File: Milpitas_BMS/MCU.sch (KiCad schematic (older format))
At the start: 74 parts, among them J100 JTAG, J101 DIAGS_UART, J102 CAN_CONN, SW100 SW_SPST, SW101 SW_SPST, U100 MIC5283-3.3ML-TR, U101 STM32F303RETx, U102 SN65HVD232

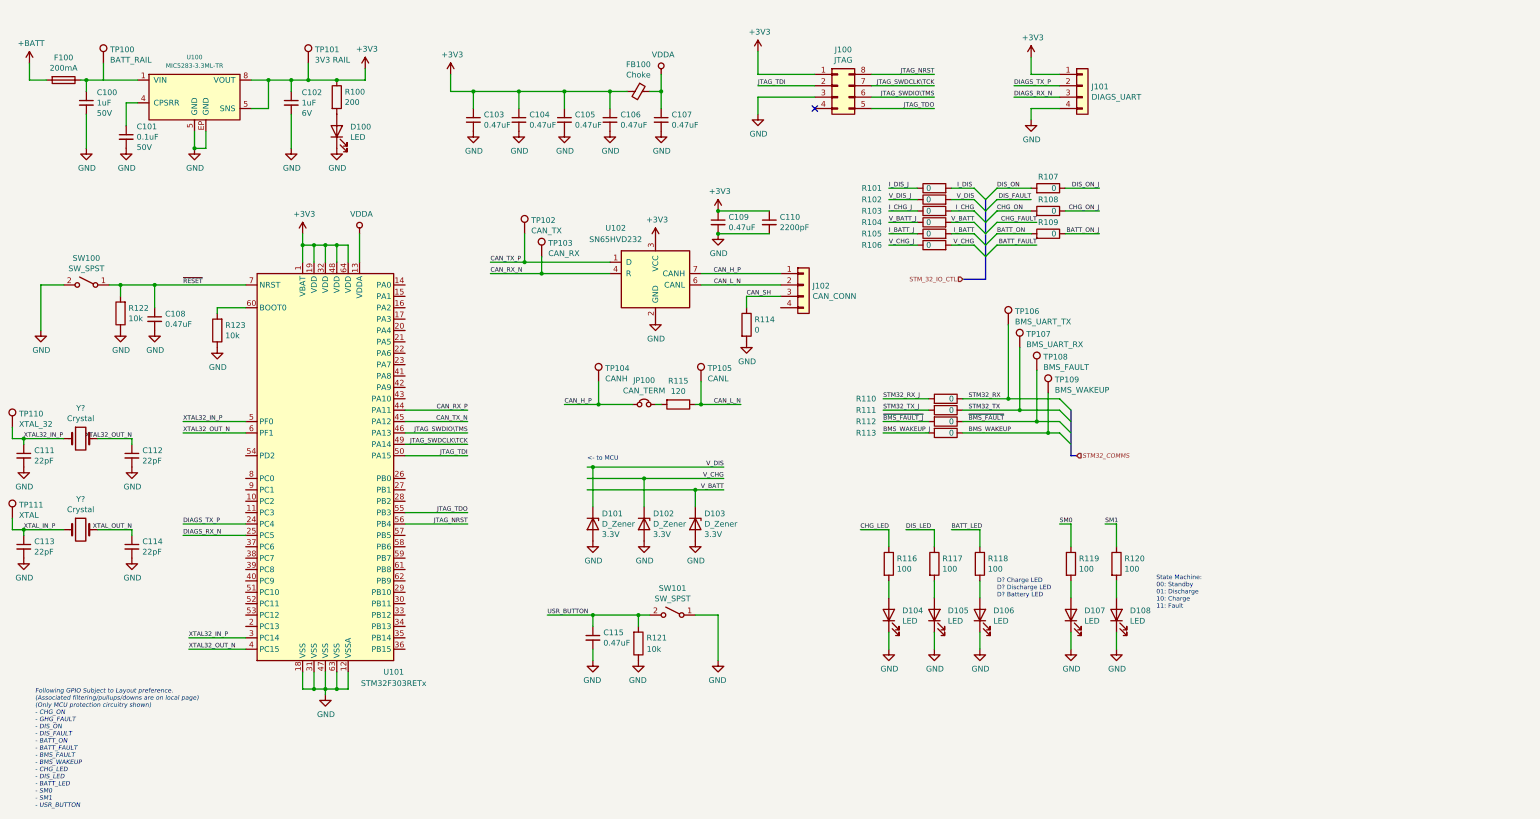
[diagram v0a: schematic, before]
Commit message: updated some parts to inclued footprints + digikey P/N
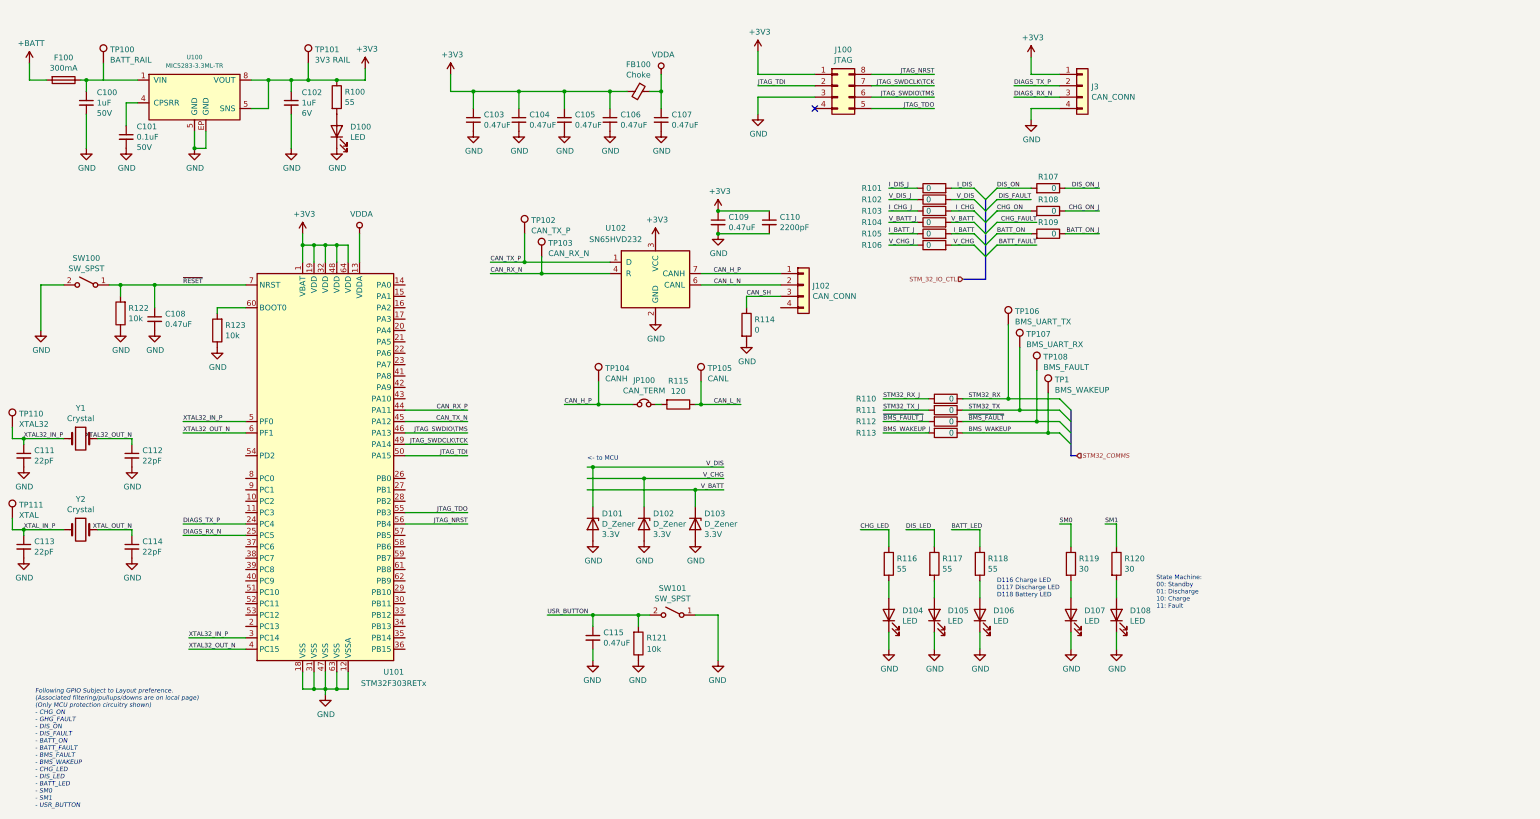
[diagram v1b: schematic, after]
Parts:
- removed J101: DIAGS_UART, symbol Connector_Generic:Conn_01x04
- removed TP109: BMS_WAKEUP, symbol Connector:TestPoint
- added J3: CAN_CONN, Connector_PinHeader_1.27mm:PinHeader_2x02_P1.27mm_Vertical, symbol Connector_Generic:Conn_01x04
- added TP1: BMS_WAKEUP, TestPoint:TestPoint_Bridge_Pitch2.54mm_Drill1.0mm, symbol Connector:TestPoint
- C100, C101, C102, C103, C104, C105, C106, C107, C108, C109, C110, C115: footprint (none) -> Capacitor_SMD:C_0603_1608Metric
- D100, D104, D105, D106: footprint (none) -> LED_SMD:LED_0603_1608Metric; Digikey (none) -> SML-D12D1WT86CT-ND
- D107, D108: footprint (none) -> LED_SMD:LED_0603_1608Metric; Digikey (none) -> 732-4978-1-ND
- F100: value 200mA -> 300mA; footprint (none) -> Fuse:Fuse_0603_1608Metric; Digikey (none) -> 507-1087-1-ND
- FB100: footprint (none) -> Inductor_SMD:L_0603_1608Metric; Digikey (none) -> 445-8672-1-ND
- J100: footprint (none) -> Connector_PinHeader_1.27mm:PinHeader_2x04_P1.27mm_Vertical; Digikey (none) -> 2057-HPH2-A-08-UA-ND
- J102: footprint (none) -> Connector_PinHeader_1.27mm:PinHeader_2x02_P1.27mm_Vertical; Digikey (none) -> 2057-HPH2-A-04-UA-ND
- JP100: footprint (none) -> Jumper:SolderJumper-2_P1.3mm_Open_TrianglePad1.0x1.5mm
- R100: value 200 -> 55; footprint (none) -> Resistor_SMD:R_0603_1608Metric
- R101, R102, R103, R104, R105, R106, R107, R108, R109, R110, R111, R112, R113, R114, R115, R121, R122, R123: footprint (none) -> Resistor_SMD:R_0603_1608Metric
- R116, R117, R118: value 100 -> 55; footprint (none) -> Resistor_SMD:R_0603_1608Metric
- R119, R120: value 100 -> 30; footprint (none) -> Resistor_SMD:R_0603_1608Metric
- TP100, TP101, TP104, TP105, TP106, TP107, TP108, TP111: footprint (none) -> TestPoint:TestPoint_Bridge_Pitch2.54mm_Drill1.0mm; Digikey (none) -> 36-5003-ND
- TP102: value CAN_TX -> CAN_TX_P; footprint (none) -> TestPoint:TestPoint_Bridge_Pitch2.54mm_Drill1.0mm; Digikey (none) -> 36-5003-ND
- TP103: value CAN_RX -> CAN_RX_N; footprint (none) -> TestPoint:TestPoint_Bridge_Pitch2.54mm_Drill1.0mm; Digikey (none) -> 36-5003-ND
- TP110: value XTAL_32 -> XTAL32; footprint (none) -> TestPoint:TestPoint_Bridge_Pitch2.54mm_Drill1.0mm; Digikey (none) -> 36-5003-ND
- U100: footprint (none) -> Package_DFN_QFN:MLF-8-1EP_3x3mm_P0.65mm_EP1.55x2.3mm_ThermalVias; Digikey (none) -> MIC5283-3.3YML-CT-ND
- gave numbers to parts that had none: 2
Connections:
- net +3V3: now also J3.1 (Pin_1)
- net BMS_WAKEUP: now also TP1.1
- net DIAGS_RX_N: now also J3.3 (Pin_3)
- net DIAGS_TX_P: now also J3.2 (Pin_2)
- net GND: now also J3.4 (Pin_4)
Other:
- note added: "D116 Charge LED\nD117 Discharge LED\nD118 Battery LED"
- note removed: "D? Charge LED\nD? Discharge LED\nD? Battery LED"

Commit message: lots of little fixes
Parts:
- added D2: D_Zener, Diode_SMD:D_SOD-323F, symbol Device:D_Zener
- added R10, R9: 0, Resistor_SMD:R_0603_1608Metric, symbol Device:R
- added R124, R125: 10k, Resistor_SMD:R_0603_1608Metric, symbol Device:R
- C111, C112: value 22pF -> 7pF; footprint (none) -> Capacitor_SMD:C_0603_1608Metric
- C113, C114: value 22pF -> 8pF; footprint (none) -> Capacitor_SMD:C_0603_1608Metric
- D101, D102, D103: footprint (none) -> Diode_SMD:D_SOD-323F; Digikey (none) -> MM3Z3V3BCT-ND
- J3: value CAN_CONN -> DIAGS_CON
- SW100, SW101: footprint (none) -> Milpitas_BMS:KSR223GLFG; Digikey (none) -> 401-1704-1-ND
- Y1: value Crystal -> 32.768kHz; footprint (none) -> Milpitas_BMS:FC-135; Digikey (none) -> FC-13532.7680KA-AG-ND
- Y2: value Crystal -> 32MHz; footprint (none) -> Milpitas_BMS:NX5032GA
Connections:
- net +3V3: now also R124.2, R125.2
- net CAN_RX_N: now also R10.1; no longer TP103.1, U102.4 (R)
- net CAN_TX_P: now also R9.1; no longer TP102.1, U102.1 (D)
- net DIAGS_RX_N: now also U101.30 (PB11), R124.1; no longer U101.25 (PC5)
- net DIAGS_TX_P: now also U101.29 (PB10), R125.1; no longer U101.24 (PC4)
- net GND: now also D2.2 (A)
- net I_CHG_J: now also D2.1 (K)
- net V_BATT_J: now also D101.1 (K)
- net V_CHG_J: now also D103.1 (K)
- net V_DIS_J: now also D102.1 (K)
- net BATT_ON renamed A11
- net CHG_ON renamed A9
- net DIS_ON renamed A7
- net I_BATT renamed A5
- net I_CHG renamed A3
- net I_DIS renamed A1
- net STM32_RX_J renamed STM32_RX_P
- net STM32_RX_P: now also U101.25 (PC5)
- net STM32_TX_J renamed STM32_TX_N
- net STM32_TX_N: now also U101.24 (PC4)
- net V_BATT renamed A4
- net A4: no longer D103.1 (K)
- net V_CHG renamed A6
- net A6: no longer D102.1 (K)
- net V_DIS renamed A2
- net A2: no longer D101.1 (K)
- new net: R9.2, TP102.1, U102.1 (D)
- new net: R10.2, TP103.1, U102.4 (R)
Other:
- moved on the sheet: J3, TP102, TP103

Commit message: For review call
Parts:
- removed J102: CAN_CONN, Connector_PinHeader_1.27mm:PinHeader_2x02_P1.27mm_Vertical, symbol Connector_Generic:Conn_01x04
- added C115: 11mF, Capacitor_SMD:C_1210_3225Metric, symbol Device:C_Small
- added D110, D111: GN, LED_SMD:LED_0603_1608Metric, symbol Device:LED
- added D112, D2, D3: PMEG6002EJ, Diode_SMD:D_SOD-323F, symbol Device:D_Small
- added D113: D_Small, Diode_SMD:D_SOD-323F, symbol Device:D_Small
- added J104: CAN_CONN, Connector_Dsub:DSUB-9_Female_Horizontal_P2.77x2.84mm_EdgePinOffset4.94mm_Housed_MountingHolesOffset7.48mm, symbol Connector_Generic:Conn_01x09
- added R126: 0, Resistor_SMD:R_0603_1608Metric, symbol Device:R
- added R127, R128: 470, Resistor_SMD:R_0603_1608Metric, symbol Device:R
- D100, D104, D105, D106: value LED -> OG
- D107, D108: value LED -> RD
- renumbered C115 to C116, D2 to D109, J3 to J102
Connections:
- net +3V3: now also D112.1 (K), D113.2 (A), D2.2 (A), D3.1 (K), R127.1, R128.1; no longer J100.1 (Pin_1), J102.1 (Pin_1), U101.1 (VBAT)
- net CAN_H_P: now also J104.2 (Pin_2), J104.5 (Pin_5)
- net CAN_L_N: now also J104.3 (Pin_3), J104.6 (Pin_6)
- net CAN_RX_N: now also D110.1 (K)
- net CAN_SH: now also J104.4 (Pin_4)
- net CAN_TX_P: now also D111.1 (K)
- net GND: now also C115.2, J104.9 (Pin_9)
- net A1 renamed I_DIS
- net A11 renamed BATT_ON
- net A2 renamed V_DIS
- net A3 renamed I_CHG
- net A4 renamed V_BATT
- net A5 renamed I_BATT
- net A6 renamed V_CHG
- net A7 renamed DIS_ON
- net A9 renamed CHG_ON
- new net: D112.2 (A), J102.1 (Pin_1)
- new net: D3.2 (A), J104.1 (Pin_1)
- new net: D2.1 (K), J100.1 (Pin_1)
- new net: D111.2 (A), R127.2
- new net: D110.2 (A), R128.2
- new net: D113.1 (K), R126.2
- new net: C115.1, R126.1, U101.1 (VBAT)
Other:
- note added: "28 AWG (1.4A max) \n1:1 Pin Mapping\nChop one end off for breakout\n10 Feet"
- note added: "E_cap = 1/2*C*V^2\nE_cap = 0.1815J\nP_RTC = 3.3 uW\nT_ON = E_cap/P_RTC\nT_ON = approx 15 hours"
- note added: "Pinout Subject to change during layout"
- moved on the sheet: C109, C110, D101, D102, D103, D109, J100, J102, JP100, R10, R101, R102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

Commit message: (maybe) final placement V1,0
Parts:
- removed TP1: BMS_WAKEUP, TestPoint:TestPoint_Bridge_Pitch2.54mm_Drill1.0mm, symbol Connector:TestPoint
- added TP109: BMS_WAKEUP, TestPoint:TestPoint_Pad_D1.0mm, symbol Connector:TestPoint
- TP100, TP102, TP106, TP107, TP108, TP110, TP111: footprint TestPoint:TestPoint_Bridge_Pitch2.54mm_Drill1.0mm -> TestPoint:TestPoint_Pad_D1.0mm; Digikey 36-5003-ND -> (none)
- TP101: value 3V3 RAIL -> 3V3_RAIL; footprint TestPoint:TestPoint_Bridge_Pitch2.54mm_Drill1.0mm -> TestPoint:TestPoint_Pad_D1.0mm; Digikey 36-5003-ND -> (none)
- TP103: footprint TestPoint:TestPoint_Bridge_Pitch2.54mm_Drill1.0mm -> TestPoint:TestPoint_Pad_D1.0mm
- renumbered D2 to D114
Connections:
- net BMS_WAKEUP: now also TP109.1
- net CAN_SH: now also J104.5 (Pin_5); no longer J104.4 (Pin_4)
- net at D112.2 (A): now also J102.2 (Pin_2); no longer J102.1 (Pin_1)
- net CAN_N: now reaches J104.8 (Pin_8)
- net CAN_N: now also J104.3 (Pin_3), R115.1, TP105.1, U102.6 (CANL)
- net CAN_H_P renamed CAN_P
- net CAN_P: now also J104.4 (Pin_4); no longer J104.5 (Pin_5)
- removed net CAN_L_N: J104.3 (Pin_3), J104.6 (Pin_6), R115.1, TP105.1, U102.6 (CANL)
- net DIAGS_RX_N renamed DIAGS_N
- net DIAGS_TX_P renamed DIAGS_P
- net DIAGS_P: now also J102.1 (Pin_1); no longer J102.2 (Pin_2)
- net STM32_RX renamed STM32_UART_P
- net STM32_RX_P renamed STM32_UART_J_P
- net STM32_TX renamed STM32_UART_N
- net STM32_TX_N renamed STM32_UART_J_N
- net XTAL32_OUT_N renamed XTAL32_IN_N
- net XTAL_IN_P renamed XTAL_P
- net XTAL_OUT_N renamed XTAL_N
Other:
- note added: "STM32_UART_P = STM32_RX\nSTM32_UART_N = STM32_TX"
- note removed: "Pinout Subject to change during layout"
- moved on the sheet: D112, J102, R114, R124, R125

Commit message: First pass routing
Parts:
- SW100, SW101: footprint Milpitas_BMS:KSR223GLFG -> Milpitas_BMS:B3U-1100P; Digikey 401-1704-1-ND -> SW1020CT-ND
- Y2: value 32MHz -> 16MHz; footprint Milpitas_BMS:NX5032GA -> Milpitas_BMS:NX3225GB; Digikey (none) -> 644-1233-1-ND
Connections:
- net CAN_RX_P is gone; now on net CAN_UART_N: U101.44 (PA11)
- net CAN_TX_P is gone; now on net CAN_UART_P: D111.1 (K), R9.1
- net BATT_FAULT: now also U101.52 (PC11)
- net BATT_LED: now also U101.39 (PC8)
- net BATT_ON_J: now also U101.51 (PC10)
- net BMS_WAKEUP_J: now also U101.27 (PB1)
- net CAN_N: now also J104.2 (Pin_2); no longer J104.3 (Pin_3)
- net CAN_P: now also J104.7 (Pin_7); no longer J104.2 (Pin_2)
- net CHG_FAULT: now also U101.58 (PB6)
- net CHG_LED: now also U101.40 (PC9)
- net CHG_ON_J: now also U101.57 (PB5)
- net DIAGS_N: now also J102.1 (Pin_1), R125.1, U101.24 (PC4); no longer J102.3 (Pin_3), R124.1, U101.30 (PB11)
- net DIAGS_P: now also J102.3 (Pin_3), R124.1, U101.25 (PC5); no longer J102.1 (Pin_1), R125.1, U101.29 (PB10)
- net DIS_FAULT: now also U101.54 (PD2)
- net DIS_LED: now also U101.41 (PA8)
- net DIS_ON_J: now also U101.53 (PC12)
- net GND: now also J100.2 (Pin_2), J104.6 (Pin_6); no longer J100.3 (Pin_3), J104.9 (Pin_9)
- net I_BATT_J: now also U101.16 (PA2)
- net I_CHG_J: now also U101.8 (PC0)
- net I_DIS_J: now also U101.14 (PA0)
- net JTAG_TDI: now also J100.3 (Pin_3); no longer J100.2 (Pin_2)
- net SM0: now also U101.42 (PA9)
- net SM1: now also U101.43 (PA10)
- net STM32_UART_J_N: now also U101.29 (PB10); no longer U101.24 (PC4)
- net STM32_UART_J_P: now also U101.30 (PB11); no longer U101.25 (PC5)
- net USR_BUTTON: now also U101.26 (PB0)
- net V_BATT_J: now also U101.17 (PA3)
- net V_CHG_J: now also U101.9 (PC1)
- net V_DIS_J: now also U101.15 (PA1)
- net XTAL_N: now also U101.6 (PF1)
- net XTAL_P: now also U101.5 (PF0)
- net ~BMS_FAULT_J: now also U101.28 (PB2)
- net at J104.1 (Pin_1): no longer D3.2 (A)
- net CAN_RX_N renamed CAN_UART_N
- net CAN_TX_N renamed CAN_UART_P
- net XTAL32_IN_N renamed XTAL32_N
- net XTAL32_N: no longer U101.6 (PF1)
- net XTAL32_IN_P renamed XTAL32_P
- net XTAL32_P: no longer U101.5 (PF0)
- new net: D3.2 (A), J104.9 (Pin_9)
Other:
- note added: "CAN_UART_P = CAN_UART_TX\nCAN_UART_N = CAN_UART_RX"
- moved on the sheet: D3, J104, R114
